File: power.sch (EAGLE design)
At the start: 126 parts, among them CN2 2X10 HEADER, Q1 IXTK180N15P, Q2 IXTK180N15P, Q3 2N7002, Q4 SPD15P10PL, Q5 2N7002, U1 LT1630, U10 LM2936, U11 LM317, U2 LT1630, U3 DCDC 15V, U4 DAC80501, U5 DAC80501, U6 ADS1120, U7 LM2662, U8 LM7805, U9 TPS3700

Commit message: Added control for the output relay
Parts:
- removed Q3: 2N7002, TRANSISTORs:2N7002P,215
- added U12: SPST SSR, ICs:CPC1002N
- R11: value 10k -> 820R; device r_0603:ERJ3EKF1002V -> r_0603:ERJ3EKF8200V
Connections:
- new net N$13: R11.2, U12.LED_A
- net DGND: now also U12.LED_K; no longer CN2.16
- net GND: now also U12.SW2; no longer Q3.S, R11.1
- net N$19: now also U12.SW1; no longer Q3.D
- net OUTPUT_RLY_EN: now also CN2.16, R11.1; no longer Q3.G, R11.2
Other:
- moved on the sheet: D1, R11, RL1A
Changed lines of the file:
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@@
 <part name="C9" library="CAPACITORS" deviceset="ECA-1EM471" device="" value="470uF 25V"/>
 <part name="L3" library="INDUCTORS" deviceset="SRR1210-470M" device="" value="47uH 3.1A"/>
-<part name="Q3" library="TRANSISTORs" deviceset="2N7002" device="P,215" value="2N7002"/>
 <part name="D1" library="DIODES" deviceset="PMEG4010BEA" device="" value="PMEG4010BEA"/>
-<part name="R11" library="r_0603" deviceset="ERJ3EKF1002V" device="" value="10k"/>
 <part name="U$11" library="NETS" deviceset="PGND" device=""/>
 <part name="U4" library="ICs" deviceset="DAC80501" device="" value="DAC80501"/>
@@
 <part name="U$71" library="NETS" deviceset="VIN" device=""/>
 <part name="GND1" library="NETS" deviceset="GND" device=""/>
-<part name="GND2" library="NETS" deviceset="GND" device=""/>
 <part name="GND3" library="NETS" deviceset="GND" device=""/>
 <part name="U$72" library="NETS" deviceset="15V" device=""/>
@@
 <part name="CN2" library="CONNECTORs" deviceset="2X10_HEADER_FEMALE" device="" value="2X10 HEADER"/>
 <part name="U$80" library="NETS" deviceset="VOUT" device=""/>
+<part name="U12" library="ICs" deviceset="CPC1002N" device="" value="SPST SSR"/>
+<part name="U$81" library="NETS" deviceset="DGND" device=""/>
+<part name="R11" library="r_0603" deviceset="ERJ3EKF8200V" device="" value="820R"/>
 </parts>
 <sheets>
@@
 <attribute name="VALUE" x="332.74" y="93.98" size="1.27" layer="96" rot="R90" align="center"/>
 </instance>
-<instance part="RL1" gate="A" x="386.08" y="58.42" smashed="yes">
-<attribute name="NAME" x="383.54" y="69.088" size="1.27" layer="95"/>
-<attribute name="VALUE" x="383.54" y="67.31" size="1.27" layer="96"/>
+<instance part="RL1" gate="A" x="414.02" y="58.42" smashed="yes">
+<attribute name="NAME" x="411.48" y="69.088" size="1.27" layer="95"/>
+<attribute name="VALUE" x="411.48" y="67.31" size="1.27" layer="96"/>
 </instance>
 <instance part="RL1" gate="B" x="347.98" y="86.36" smashed="yes">
@@
 <attribute name="VALUE" x="340.36" y="184.15" size="1.27" layer="96" align="center"/>
 </instance>
-<instance part="Q3" gate="G$1" x="378.46" y="43.18" smashed="yes">
-<attribute name="NAME" x="379.73" y="45.72" size="1.27" layer="95"/>
-<attribute name="VALUE" x="379.73" y="43.18" size="1.27" layer="96"/>
-</instance>
-<instance part="D1" gate="G$1" x="378.46" y="58.42" smashed="yes" rot="R90">
-<attribute name="NAME" x="375.92" y="58.42" size="1.27" layer="95" rot="R90" align="center"/>
-<attribute name="VALUE" x="381" y="58.42" size="1.27" layer="96" rot="R90" align="center"/>
-</instance>
-<instance part="R11" gate="G$1" x="370.84" y="35.56" smashed="yes" rot="R90">
-<attribute name="NAME" x="368.3" y="35.56" size="1.27" layer="95" rot="R90" align="center"/>
-<attribute name="VALUE" x="373.38" y="35.56" size="1.27" layer="96" rot="R90" align="center"/>
+<instance part="D1" gate="G$1" x="406.4" y="58.42" smashed="yes" rot="R90">
+<attribute name="NAME" x="403.86" y="58.42" size="1.27" layer="95" rot="R90" align="center"/>
+<attribute name="VALUE" x="408.94" y="58.42" size="1.27" layer="96" rot="R90" align="center"/>
 </instance>
 <instance part="U$11" gate="G$1" x="86.36" y="434.34" smashed="yes">
@@
 <attribute name="VALUE" x="175.26" y="447.04" size="1.778" layer="96" align="center"/>
 </instance>
-<instance part="GND2" gate="G$1" x="370.84" y="25.4" smashed="yes">
-<attribute name="VALUE" x="370.84" y="22.86" size="1.778" layer="96" align="center"/>
-</instance>
-<instance part="GND3" gate="G$1" x="378.46" y="35.56" smashed="yes">
-<attribute name="VALUE" x="378.46" y="33.02" size="1.778" layer="96" align="center"/>
+<instance part="GND3" gate="G$1" x="406.4" y="33.02" smashed="yes">
+<attribute name="VALUE" x="406.4" y="30.48" size="1.778" layer="96" align="center"/>
 </instance>
 <instance part="U$72" gate="G$1" x="175.26" y="474.98" smashed="yes">
 <attribute name="VALUE" x="175.26" y="477.52" size="1.778" layer="96" rot="R180" align="center"/>
 </instance>
-<instance part="U$73" gate="G$1" x="378.46" y="71.12" smashed="yes">
-<attribute name="VALUE" x="378.46" y="73.66" size="1.778" layer="96" rot="R180" align="center"/>
+<instance part="U$73" gate="G$1" x="406.4" y="71.12" smashed="yes">
+<attribute name="VALUE" x="406.4" y="73.66" size="1.778" layer="96" rot="R180" align="center"/>
 </instance>
 <instance part="U$9" gate="G$1" x="193.04" y="205.74" smashed="yes">
@@
 <instance part="U$80" gate="G$1" x="137.16" y="474.98" smashed="yes">
 <attribute name="VALUE" x="137.16" y="477.52" size="1.778" layer="96" rot="R180" align="center"/>
+</instance>
+<instance part="U12" gate="G$1" x="391.16" y="43.18" smashed="yes">
+<attribute name="NAME" x="383.54" y="55.88" size="1.778" layer="95"/>
+<attribute name="VALUE" x="383.54" y="53.34" size="1.778" layer="96"/>
+</instance>
+<instance part="U$81" gate="G$1" x="375.92" y="33.02" smashed="yes">
+<attribute name="VALUE" x="375.92" y="30.48" size="1.778" layer="96" align="center"/>
+</instance>
+<instance part="R11" gate="G$1" x="370.84" y="48.26" smashed="yes">
+<attribute name="NAME" x="370.84" y="50.8" size="1.27" layer="95" align="center"/>
+<attribute name="VALUE" x="370.84" y="45.72" size="1.27" layer="96" align="center"/>
 </instance>
 </instances>
@@
 <segment>
 <pinref part="RL1" gate="A" pin="A2"/>
-<wire x1="381" y1="50.8" x2="378.46" y2="50.8" width="0.1524" layer="91"/>
-<wire x1="378.46" y1="50.8" x2="378.46" y2="53.34" width="0.1524" layer="91"/>
-<wire x1="378.46" y1="50.8" x2="378.46" y2="48.26" width="0.1524" layer="91"/>
-<junction x="378.46" y="50.8"/>
-<pinref part="Q3" gate="G$1" pin="D"/>
+<wire x1="408.94" y1="50.8" x2="406.4" y2="50.8" width="0.1524" layer="91"/>
+<wire x1="406.4" y1="50.8" x2="406.4" y2="53.34" width="0.1524" layer="91"/>
+<wire x1="406.4" y1="50.8" x2="406.4" y2="48.26" width="0.1524" layer="91"/>
+<junction x="406.4" y="50.8"/>
 <pinref part="D1" gate="G$1" pin="A"/>
+<pinref part="U12" gate="G$1" pin="SW1"/>
+<wire x1="406.4" y1="48.26" x2="403.86" y2="48.26" width="0.1524" layer="91"/>
 </segment>
 </net>
 <net name="OUTPUT_RLY_EN" class="0">
 <segment>
-<pinref part="Q3" gate="G$1" pin="G"/>
-<wire x1="373.38" y1="43.18" x2="370.84" y2="43.18" width="0.1524" layer="91"/>
-<pinref part="R11" gate="G$1" pin="2"/>
-<wire x1="370.84" y1="43.18" x2="345.44" y2="43.18" width="0.1524" layer="91"/>
-<wire x1="370.84" y1="40.64" x2="370.84" y2="43.18" width="0.1524" layer="91"/>
-<junction x="370.84" y="43.18"/>
-<label x="347.98" y="43.18" size="1.778" layer="95"/>
+<label x="342.9" y="48.26" size="1.778" layer="95"/>
+<wire x1="365.76" y1="48.26" x2="340.36" y2="48.26" width="0.1524" layer="91"/>
+<pinref part="R11" gate="G$1" pin="1"/>
+</segment>
+<segment>
+<pinref part="CN2" gate="G$1" pin="16"/>
+<wire x1="12.7" y1="264.16" x2="40.64" y2="264.16" width="0.1524" layer="91"/>
+<label x="15.24" y="264.16" size="1.778" layer="95"/>
 </segment>
 </net>
@@
 </segment>
 <segment>
-<pinref part="CN2" gate="G$1" pin="16"/>
-<wire x1="12.7" y1="264.16" x2="40.64" y2="264.16" width="0.1524" layer="91"/>
-<label x="15.24" y="264.16" size="1.778" layer="95"/>
+<pinref part="U12" gate="G$1" pin="LED_K"/>
+<wire x1="378.46" y1="38.1" x2="375.92" y2="38.1" width="0.1524" layer="91"/>
+<pinref part="U$81" gate="G$1" pin="DGND"/>
+<wire x1="375.92" y1="38.1" x2="375.92" y2="35.56" width="0.1524" layer="91"/>
 </segment>
 </net>
@@
 <net name="GND" class="0">
 <segment>
-<pinref part="R11" gate="G$1" pin="1"/>
-<pinref part="GND2" gate="G$1" pin="GND"/>
-<wire x1="370.84" y1="27.94" x2="370.84" y2="30.48" width="0.1524" layer="91"/>
-</segment>
-<segment>
-<pinref part="Q3" gate="G$1" pin="S"/>
 <pinref part="GND3" gate="G$1" pin="GND"/>
-<wire x1="378.46" y1="38.1" x2="378.46" y2="40.64" width="0.1524" layer="91"/>
+<wire x1="406.4" y1="35.56" x2="406.4" y2="38.1" width="0.1524" layer="91"/>
+<pinref part="U12" gate="G$1" pin="SW2"/>
+<wire x1="406.4" y1="38.1" x2="403.86" y2="38.1" width="0.1524" layer="91"/>
 </segment>
 <segment>
@@
 </segment>
 <segment>
-<wire x1="378.46" y1="68.58" x2="378.46" y2="66.04" width="0.1524" layer="91"/>
+<wire x1="406.4" y1="68.58" x2="406.4" y2="66.04" width="0.1524" layer="91"/>
 <pinref part="RL1" gate="A" pin="A1"/>
-<wire x1="378.46" y1="66.04" x2="378.46" y2="63.5" width="0.1524" layer="91"/>
-<wire x1="381" y1="66.04" x2="378.46" y2="66.04" width="0.1524" layer="91"/>
-<junction x="378.46" y="66.04"/>
+<wire x1="406.4" y1="66.04" x2="406.4" y2="63.5" width="0.1524" layer="91"/>
+<wire x1="408.94" y1="66.04" x2="406.4" y2="66.04" width="0.1524" layer="91"/>
+<junction x="406.4" y="66.04"/>
 <pinref part="D1" gate="G$1" pin="K"/>
 <pinref part="U$73" gate="G$1" pin="15V"/>
@@
 </segment>
 </net>
+<net name="N$13" class="0">
+<segment>
+<pinref part="U12" gate="G$1" pin="LED_A"/>
+<pinref part="R11" gate="G$1" pin="2"/>
+<wire x1="378.46" y1="48.26" x2="375.92" y2="48.26" width="0.1524" layer="91"/>
+</segment>
+</net>

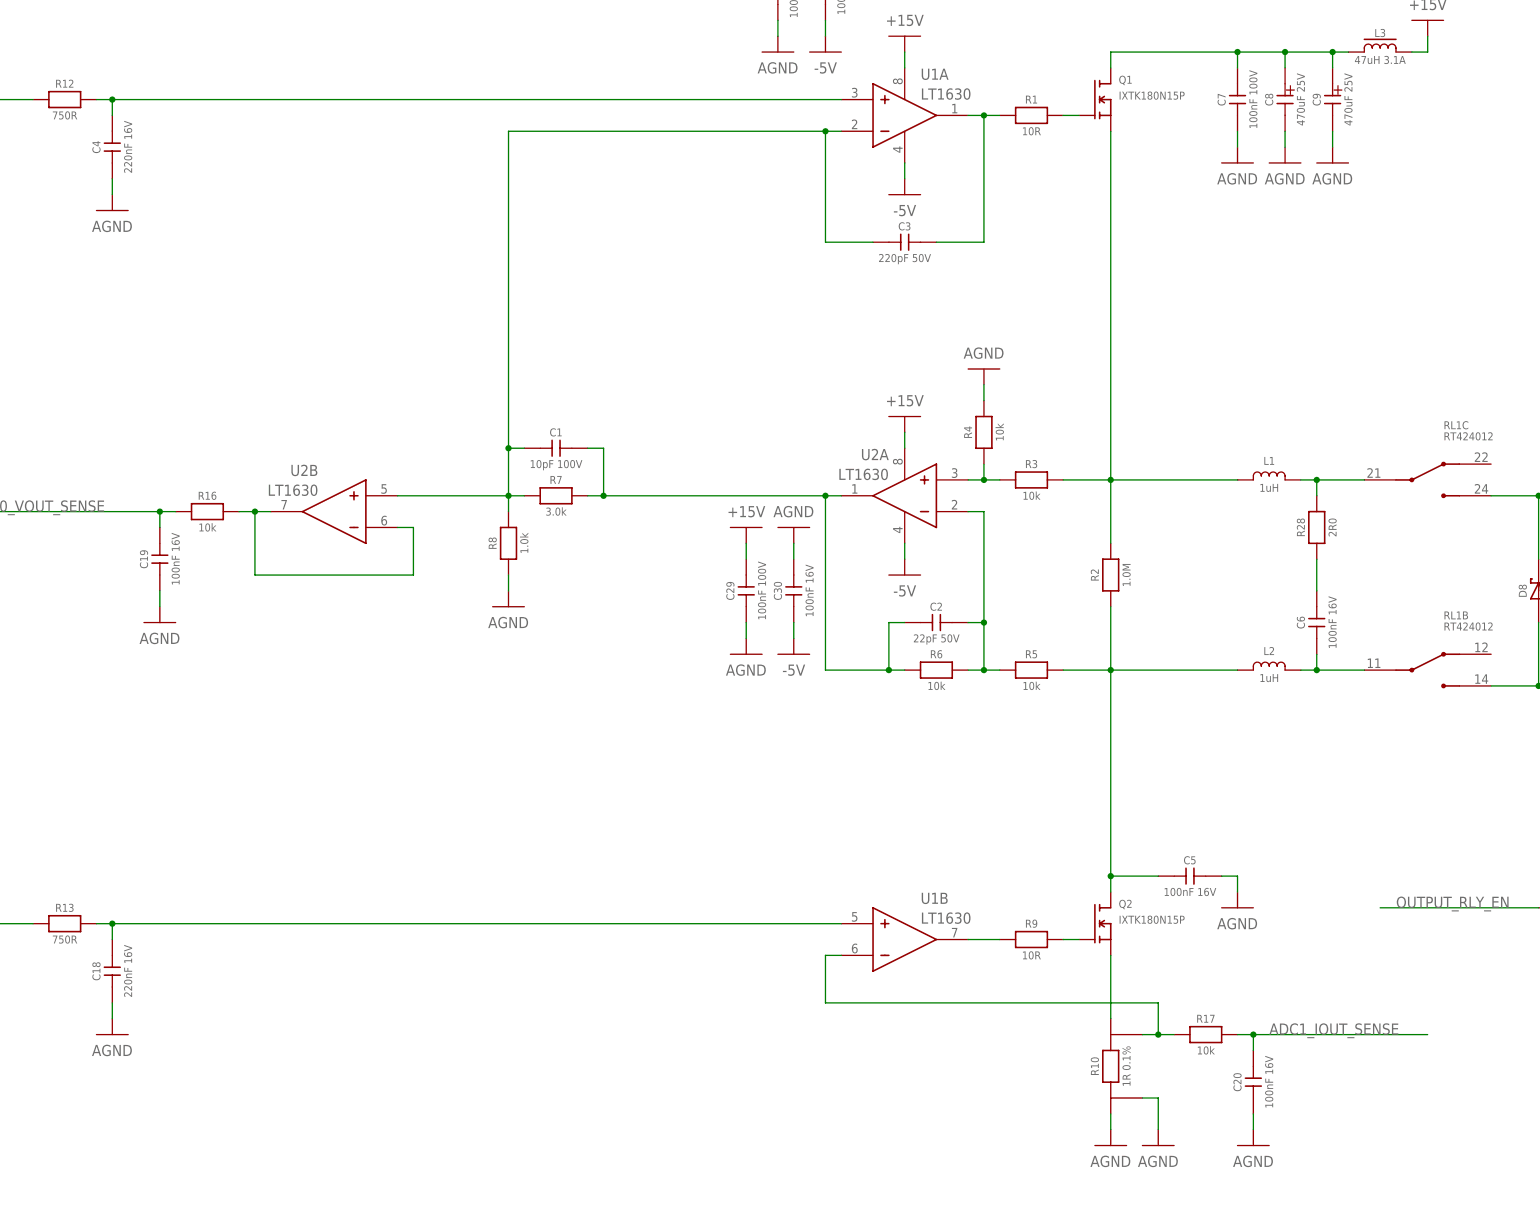
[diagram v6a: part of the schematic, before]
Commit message: Fixes for stability
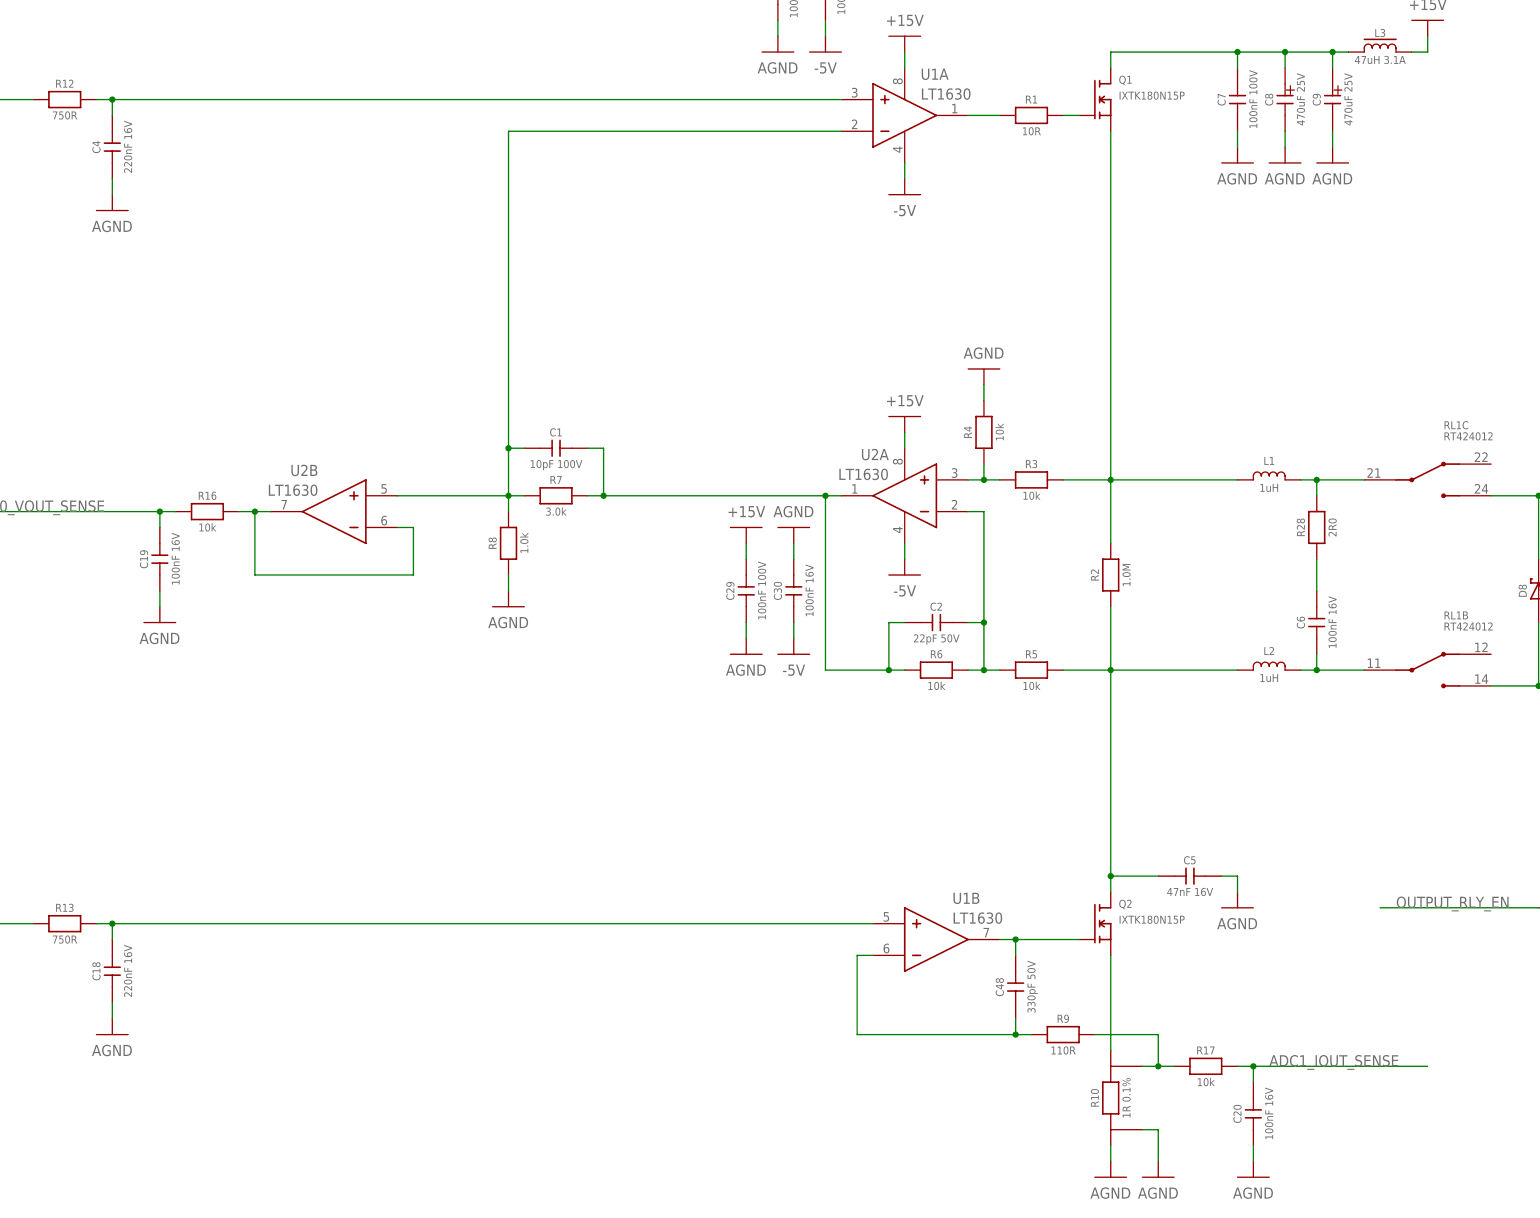
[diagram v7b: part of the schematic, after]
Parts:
- removed C3: 220pF 50V, CAPACITORS:CC0603JRNPO9BN221
- added C48: 330pF 50V, CAPACITORS:CC0603JRNPO9BN331
- C5: value 100nF 16V -> 47nF 16V; device CAPACITORS:CL10B104KO8WPNC -> CAPACITORS:CL10B473KO8NNNC
- R9: value 10R -> 110R; device r_0603:ERJ3EKF10R0V -> r_0603:ERJ3EKF1100V
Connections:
- net N$1: no longer C3.2
- net N$11: now also C48.1, R9.1, U1B.-; no longer Q2.G, R9.2
- net N$345: no longer C3.1
- net N$76: now also R9.2; no longer U1B.-
- net N$9: now also C48.2, Q2.G; no longer R9.1
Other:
- moved on the sheet: C20, R10, R17, R9, U1B
